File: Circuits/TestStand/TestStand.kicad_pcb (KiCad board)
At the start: 2 copper layers, 92.5 x 137.5 mm, 111 parts, among them IC1 STP85NF55, J1 Screw_Terminal_01x07, J10 Screw_Terminal_01x03, J11 Screw_Terminal_01x03, J12 Screw_Terminal_01x03, J13 Screw_Terminal_01x03, J14 Screw_Terminal_01x02, J15 Conn_Coaxial, J16 Screw_Terminal_01x02, J17 Screw_Terminal_01x02, J2 Screw_Terminal_01x07, J3 Screw_Terminal_01x07, J4 Screw_Terminal_01x03, J5 Screw_Terminal_01x03, J6 Screw_Terminal_01x03, J7 Screw_Terminal_01x03, J8 Screw_Terminal_01x03, J9 Screw_Terminal_01x03, Q1 MMBT4403-7-F, Q2 MMBT4403-7-F, Q3 MMBT4403-7-F, SW1 SW_DIP_x01, U1 HX711, U2 HX711, U3 HX711, U4 Teensy4.1, U5 LP2980IM5X-3.3/NOPB, U6 MAX31855KASA, U7 NRF24L01, U8 LP2980IM5X-3.3/NOPB, Y1 16Mhz

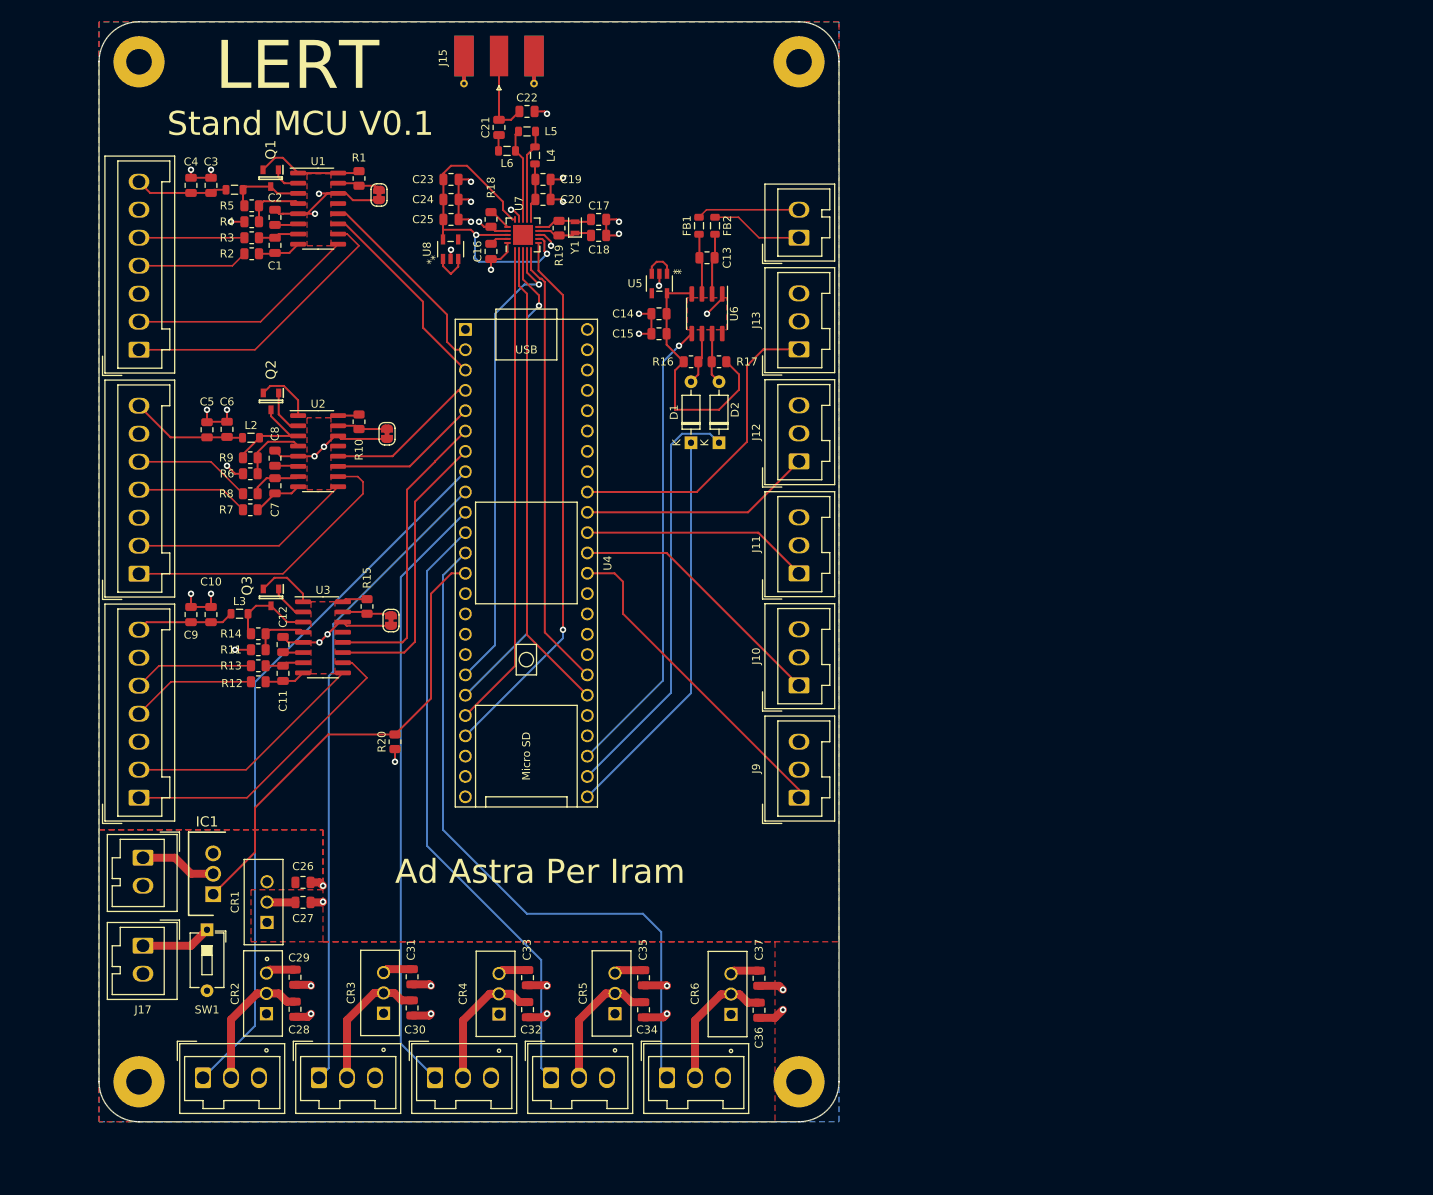
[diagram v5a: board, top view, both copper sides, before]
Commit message: Very important silkscreen additions
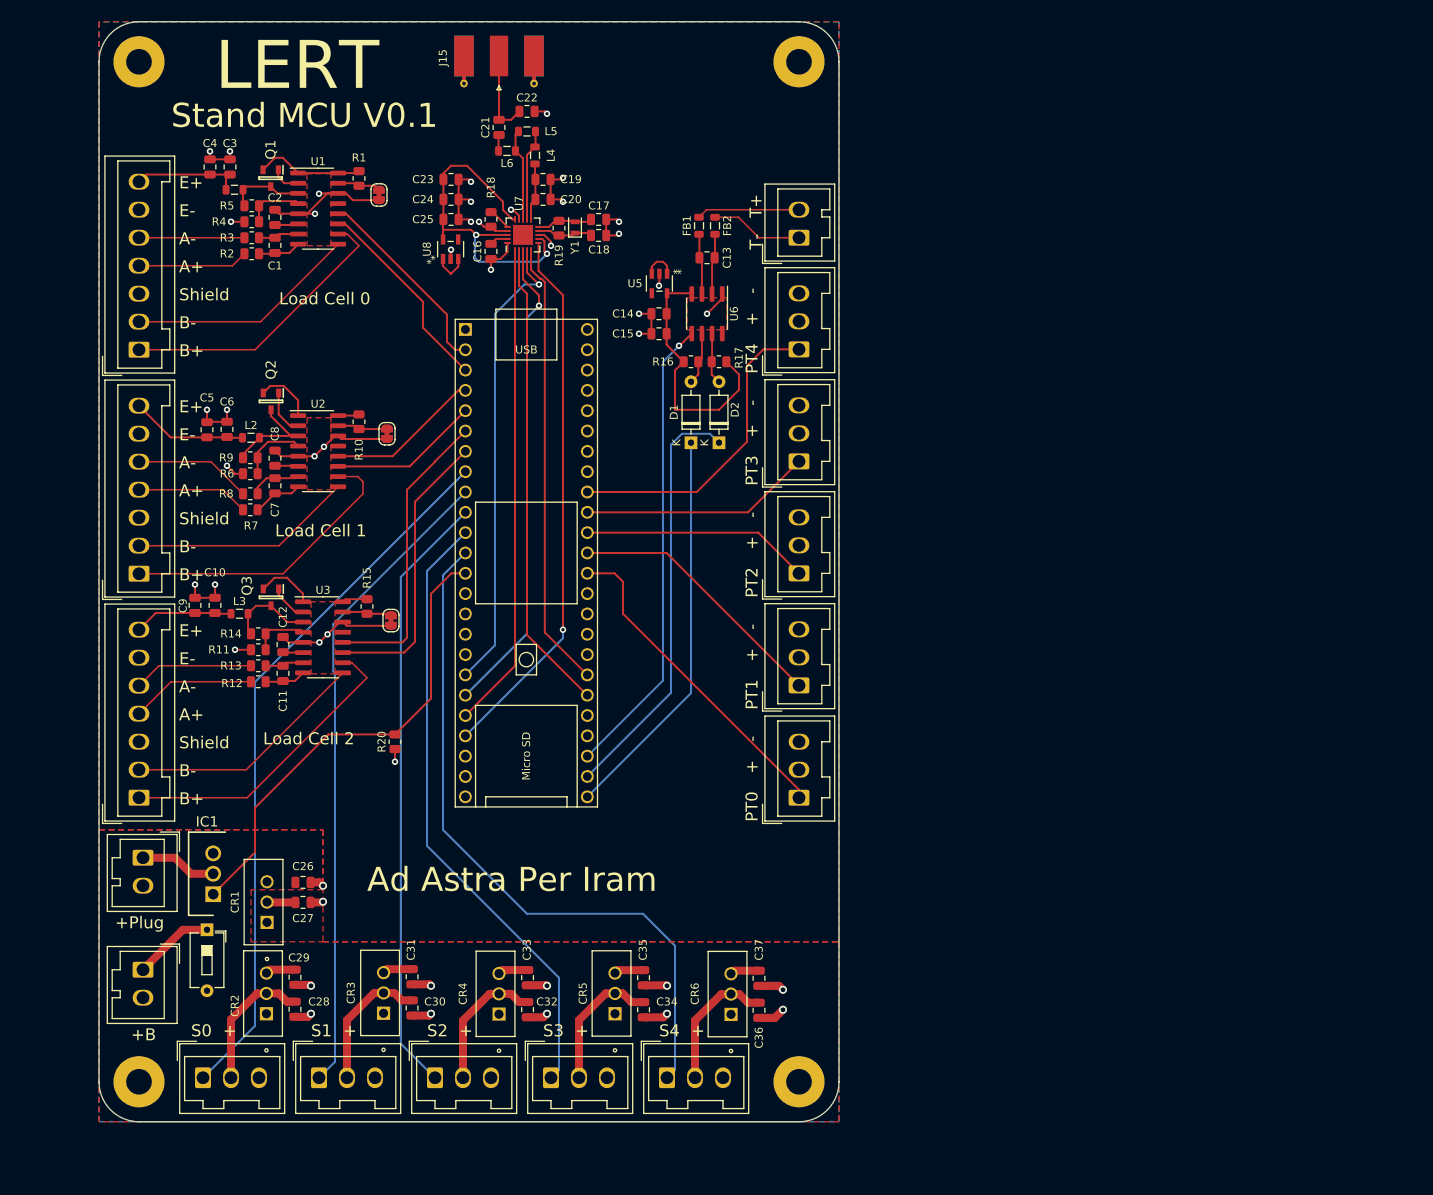
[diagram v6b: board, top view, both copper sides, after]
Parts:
- moved C3 3.31 mm to (38.9, 81.2)
- moved C4 3.31 mm to (36.4, 81.2)
- moved J17 3.00 mm to (28.0, 181.5)
- moved C10 1.25 mm to (37.0, 135.9)
- moved C9 1.25 mm to (34.5, 135.9)
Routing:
- net /E+: track 11.6 -> 13.9 mm
- net Net-(J17-Pin_1): track 8.83 -> 10.1 mm
- net /PWM4: track 86.9 -> 87.7 mm
- net /PWM3: track 76.5 -> 77.4 mm
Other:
- board text added: "+"
- board text added: "+B"
- board text added: "+Plug"
- board text added: "-"
- board text added: ":3"
- board text added: "A+"
- board text added: "A-"
- board text added: "B+"
- board text added: "B-"
- board text added: "E+"
- board text added: "E-"
- board text added: "Load Cell 0"
- board text added: "Load Cell 1"
- board text added: "Load Cell 2"
- board text added: "PT0"
- board text added: "PT1"
- board text added: "PT2"
- board text added: "PT3"
- board text added: "PT4"
- board text added: "S0"
- board text added: "S1"
- board text added: "S2"
- board text added: "S3"
- board text added: "S4"
- board text added: "Shield"
- board text added: "T+"
- board text added: "T-"

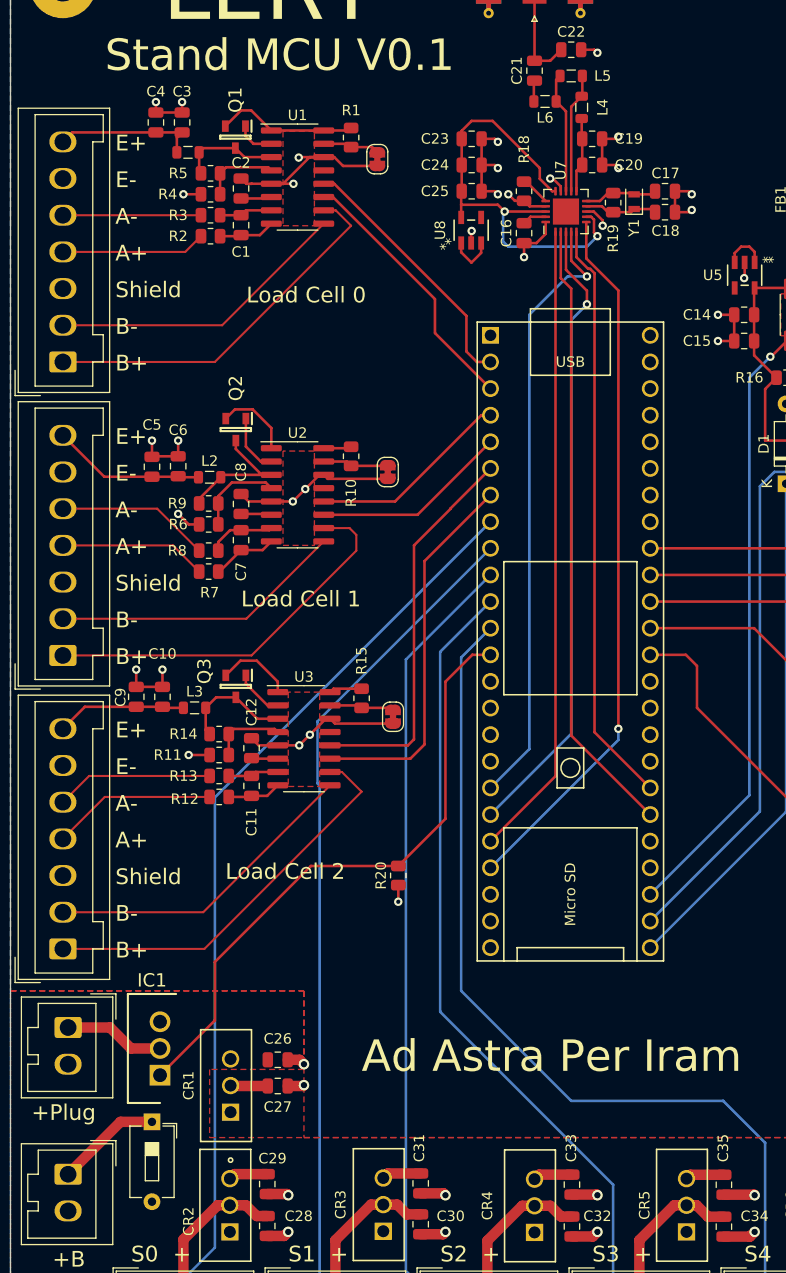
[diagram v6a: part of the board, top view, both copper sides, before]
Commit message: assigned a bunch of components to real ones
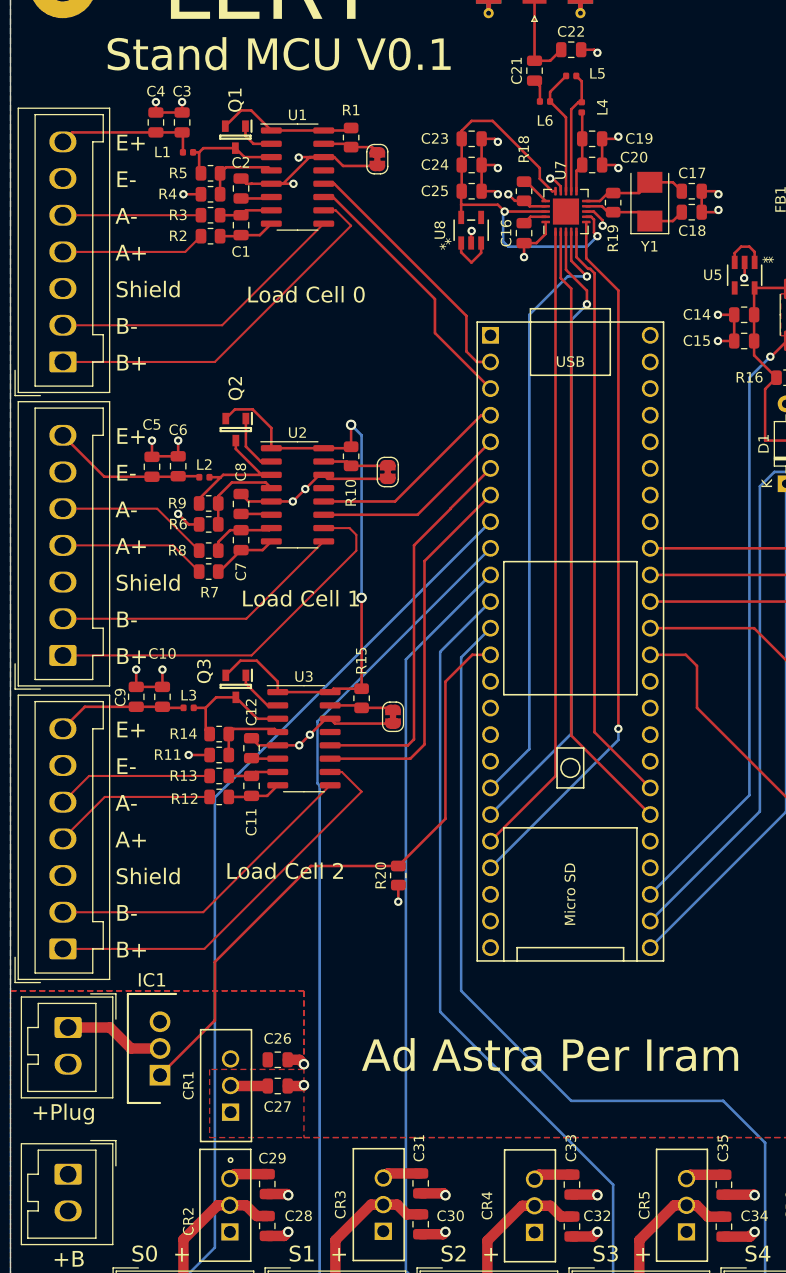
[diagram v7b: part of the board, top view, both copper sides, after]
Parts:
- removed SW1: SW_DIP_x01, Button_Switch_THT:SW_DIP_SPSTx01_Slide_6.7x4.1mm_W7.62mm_P2.54mm_LowProfile
- L1, L2, L3, L4, L5, L6: footprint Inductor_SMD:L_0805_2012Metric -> Inductor_SMD:L_0402_1005Metric
- Y1: footprint Crystal:Crystal_SMD_2012-2Pin_2.0x1.2mm -> Crystal:Crystal_SMD_5032-2Pin_5.0x3.2mm
- moved C17 2.55 mm to (87.5, 87.7)
- moved C18 2.55 mm to (87.5, 89.7)
- moved Y1 1.50 mm to (83.5, 88.7)
- moved L3 0.56 mm to (39.5, 137.0)
- moved L2 0.50 mm to (41.0, 115.0)
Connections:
- J17 pad 1: Net-(J17-Pin_1) -> GND
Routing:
- net +5V: track 46.4 -> 84.1 mm, vias 0 -> 2
- net Net-(J17-Pin_1): track 10.1 -> 0.00 mm
- net Net-(U7-XC1): track 7.05 -> 9.70 mm
- net Net-(U7-XC2): track 7.04 -> 9.55 mm
- net Net-(U3-AVDD): track 10.8 -> 11.9 mm
- net Net-(U2-AVDD): track 13.5 -> 14.6 mm
- net Net-(U7-ANT2): track 11.5 -> 12.3 mm
- net Net-(U7-VDD_PA): track 7.19 -> 7.83 mm
- net Net-(U1-AVDD): track 9.48 -> 10.1 mm

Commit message: switched to the true connectors, did some rearranging, largely backwards progress :)
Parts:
- removed J16, J17: Screw_Terminal_01x02, Connector_Wago:Wago_734-132_1x02_P3.50mm_Vertical
- added J18: 2601-1107, Library:CONN7_2601-1107_WAG, F.Cu at (26.0, 83.0)
- J1, J2: value Screw_Terminal_01x07 -> 2601-1107; footprint Connector_Wago:Wago_734-137_1x07_P3.50mm_Vertical -> Library:CONN7_2601-1107_WAG
- J10, J11, J12, J13, J4, J5, J6, J7, J8, J9: footprint Connector_Wago:Wago_734-133_1x03_P3.50mm_Vertical -> Library:CONN3_2601-1103_WAG
- J14: value Screw_Terminal_01x02 -> CONN4_2606-1104/010-000_WAG; footprint Connector_Wago:Wago_734-132_1x02_P3.50mm_Vertical -> Library:2606-1104&slash_010-000
- J3: value Screw_Terminal_01x07 -> Screw_Terminal_01x03; footprint Connector_Wago:Wago_734-137_1x07_P3.50mm_Vertical -> Library:CONN3_2601-1103_WAG
- moved J14 116.6 mm to (22.0, 166.5), turned to -90 degrees
- moved J3 102.0 mm to (110.0, 100.0)
- moved IC1 10.7 mm to (44.0, 164.1)
- moved R2 9.27 mm to (44.7, 100.7)
- moved R3 9.27 mm to (44.7, 98.7)
- moved R4 9.27 mm to (44.7, 96.7)
- moved R5 9.27 mm to (44.7, 94.7)
- moved C1 9.27 mm to (47.6, 99.7)
- moved C2 9.27 mm to (47.6, 96.2)
- moved C3 9.27 mm to (42.0, 89.9)
- moved C4 9.27 mm to (39.5, 89.9)
- moved JP1 9.27 mm to (60.6, 93.4)
- moved L1 9.27 mm to (42.5, 92.7)
- moved Q1 9.27 mm to (47.1, 91.3)
- moved R1 9.27 mm to (58.1, 91.3)
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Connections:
- FB1 pad 1: /T+ -> Net-(J3-1_1)
- IC1 pad 2: Net-(IC1-D) -> /DRAIN
- J1 pad 1: /B+ -> /E1+
- J1 pad 2: /B- -> /E1+
- J1 pad 4: /A+ -> GND
- J1 pad 5: /A- -> /A1-
- J1 pad 6: GND -> /A1-
- J1 pad 7: /E+ -> /A1+
- J10 pad 2: +5V -> /PT1
- J10 pad 3: GND -> +5V
- J11 pad 2: +5V -> /PT2
- J11 pad 3: GND -> +5V
- J12 pad 2: +5V -> /PT3
- J12 pad 3: GND -> +5V
- J13 pad 2: +5V -> /PT4
- J13 pad 3: GND -> +5V
- J14 pad 1: /T- -> +BATT
- J14 pad 2: /T+ -> GND
- J2 pad 1: /B1+ -> /E2+
- J2 pad 2: /B1- -> /E2+
- J2 pad 4: /A1+ -> GND
- J2 pad 5: /A1- -> /A2-
- J2 pad 6: GND -> /A2-
- J2 pad 7: /E1+ -> /A2+
- J3 pad 1: /B2+ -> Net-(J3-1_1)
- J3 pad 2: /B2- -> Net-(J3-1_1)
- J3 pad 3: GND -> /T-
- J3 pad 4: /A2+ -> /T-
- J3 pad 5: /A2- -> unconnected-(J3-3_1-Pad5)
- J3 pad 6: GND -> unconnected-(J3-3_2-Pad6)
- J4 pad 2: /+S0 -> /PWM0
- J4 pad 3: GND -> /+S0
- J5 pad 2: /+S1 -> /PWM1
- J5 pad 3: GND -> /+S1
- J6 pad 2: /+S2 -> /PWM2
- J6 pad 3: GND -> /+S2
- J7 pad 2: /+S3 -> /PWM3
- J7 pad 3: GND -> /+S3
- J8 pad 2: /+S4 -> /PWM4
- J8 pad 3: GND -> /+S4
- J9 pad 2: +5V -> /PT0
- J9 pad 3: GND -> +5V
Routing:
- net GND: track 150.9 -> 0.00 mm, vias 45 -> 0
- net /PWM4: track 87.7 -> 0.00 mm
- net /PWM0: track 89.3 -> 5.00 mm
- net +5V: track 84.1 -> 0.00 mm, vias 2 -> 0
- net /PWM1: track 81.0 -> 5.00 mm
- net /PWM3: track 77.4 -> 5.00 mm
- net /PWM2: track 75.9 -> 5.00 mm
- net /rIRQ: track 67.9 -> 0.00 mm, vias 1 -> 0
- net /rCE: track 60.7 -> 0.00 mm
- net /rSCK: track 60.2 -> 0.00 mm, vias 1 -> 0
- net /rCSN: track 59.1 -> 0.00 mm
- net /GP: track 59.1 -> 0.00 mm
- net /rMOSI: track 58.6 -> 0.00 mm, vias 1 -> 0
- net /tcSCK: track 58.3 -> 0.00 mm, vias 1 -> 0
- net /rMISO: track 56.1 -> 0.00 mm
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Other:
- board size 92.5 x 137.5 mm -> 105 x 142.5 mm
- board text removed: ":3"
- board text removed: "Ad Astra Per Iram"
- board text removed: "LERT"
- board text removed: "Stand MCU V0.1"
